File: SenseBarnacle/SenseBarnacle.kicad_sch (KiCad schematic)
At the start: 93 parts, among them J1 USB_B_Mini, J2 Debug, J4 Barrel_Jack, J5 I2C_OLED_Display, J6 Conn_02x35_JumperluxCardEdge, J7 Conn_02x35_JumperluxCardEdge, SW1 USB BOOT, U1 LM324, U13 CH446X, U14 CH446X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

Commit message: started routing
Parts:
- removed R5, R6: 0R, Resistor_SMD:R_0402_1005Metric, symbol JumperlessSymbols:R_Small_US_2
- removed TP17: GPIO_19, symbol Connector:TestPoint
- removed TP18: GPIO_22, symbol Connector:TestPoint
- removed TP19: GPIO_23, symbol Connector:TestPoint
- removed TP8: UART_Rx, symbol Connector:TestPoint
- removed TP9: UART_Tx, symbol Connector:TestPoint
- added C18, C19, C20, C23, C25: 0.1uF, Capacitor_SMD:C_0603_1608Metric_Pad1.08x0.95mm_HandSolder, symbol JumperlessSymbols:C_Small
- added J3: Power, Connector_PinHeader_2.54mm:PinHeader_1x05_P2.54mm_Vertical, symbol Connector:Conn_01x05_Socket
- added R29, R31, R33, R37, R5: 47K, Resistor_SMD:R_0805_2012Metric_Pad1.20x1.40mm_HandSolder, symbol JumperlessSymbols:R_Small_US_3
- added R30, R32, R34, R38, R6: 10K, Resistor_SMD:R_0805_2012Metric_Pad1.20x1.40mm_HandSolder, symbol JumperlessSymbols:R_Small_US_3
- added R35, R36: 2.2K, Resistor_SMD:R_0805_2012Metric_Pad1.20x1.40mm_HandSolder, symbol JumperlessSymbols:R_Small_US_3
- added U4: ~, JumperlessFootprints:Directional_Switch_SKRHADE010, symbol JumperlessSymbols:Switch_Multidirectional
- C1, C13, C2, C8: footprint Capacitor_SMD:C_0603_1608Metric -> Capacitor_SMD:C_0805_2012Metric_Pad1.18x1.45mm_HandSolder
- C10, C11, C12, C3, C4, C5, C9: footprint Capacitor_SMD:C_0402_1005Metric -> Capacitor_SMD:C_0603_1608Metric_Pad1.08x0.95mm_HandSolder
- C21, C22: footprint (none) -> Capacitor_SMD:C_0805_2012Metric_Pad1.18x1.45mm_HandSolder
- J4: footprint (none) -> Connector_BarrelJack:BarrelJack_CUI_PJ-063AH_Horizontal
- J5: footprint (none) -> Connector_PinHeader_2.54mm:PinHeader_1x04_P2.54mm_Vertical
- J6: footprint JumperlessFootprints:HEE70LP03BK_Daughter_Penis -> JumperlessFootprints:HEE70LP03BK_Daughter_Penis_Top
- JP1, JP6: footprint (none) -> JumperlessFootprints:SolderJumper_2_Open_Small
- JP2, JP3, JP4, JP5: footprint (none) -> Jumper:SolderJumper-3_P1.3mm_Bridged2Bar12_RoundedPad1.0x1.5mm
- JP7: footprint (none) -> JumperlessFootprints:SolderJumper_2_Bridged_Small
- R1, R2: footprint Resistor_SMD:R_0402_1005Metric -> Resistor_SMD:R_0402_1005Metric_Pad0.72x0.64mm_HandSolder
- R10, R11, R12, R13, R14, R15, R16, R17, R27, R28: footprint Resistor_SMD:R_0402_1005Metric -> Resistor_SMD:R_0805_2012Metric_Pad1.20x1.40mm_HandSolder
- R18, R19, R20, R21, R22, R23, R24, R25, R26, R3, R8, R9: footprint (none) -> Resistor_SMD:R_0805_2012Metric_Pad1.20x1.40mm_HandSolder
- R4, R7: footprint Resistor_SMD:R_0402_1005Metric -> Resistor_SMD:R_0603_1608Metric_Pad0.98x0.95mm_HandSolder
- TP1, TP10, TP11, TP12, TP14, TP15, TP2, TP20, TP21, TP3, TP4, TP5: footprint (none) -> JumperlessFootprints:TestPoint_D0.75mm
- TP13, TP6, TP7: footprint (none) -> JumperlessFootprints:PINHEADER-1x1_vertical
- TP16: value GPIO_4 -> GPIO_2; footprint (none) -> JumperlessFootprints:TestPoint_D0.75mm
- U1, U2: footprint (none) -> JumperlessFootprints:SOIC-14_3.9x8.7mm_P1.27mm
- U12: footprint (none) -> JumperlessFootprints:QA503C
- U13, U14, U15: footprint (none) -> JumperlessFootprints:LQFP44_Tight
- U6: footprint AK4619VN_AKM -> JumperlessFootprints:AK4619VN_AKM
- U9: footprint RP2040_minimal:RP2040-QFN-56 -> JumperlessFootprints:RP2040-QFN-56
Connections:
- net +18V: now also J3.5 (Pin_5)
- net +3V3: now also J3.2 (Pin_2), R29.2, R31.2, R33.2, R35.1, R36.1, R37.2, R5.2
- net +5V: now also J3.1 (Pin_1)
- net -3.5V: now also J3.4 (Pin_4)
- net GND: now also C18.2, C19.2, C20.2, C23.2, C25.2, J3.3 (Pin_3), U4.5 (Common)
- net I2C_SCL: now also R36.2
- net I2C_SDA: now also R35.2
- net at U9.3 (GPIO1): now also R28.1
- net at U9.2 (GPIO0): now also R27.1
- net GPI0_2: now reaches U9.4 (GPIO2)
- net GPI0_2: now also TP16.1; no longer R27.1
- net SW_A: now reaches U9.5 (GPIO3)
- net SW_A: now also C18.1, R6.1; no longer R28.1
- net GPI0_19 renamed SW_PUSH
- net SW_PUSH: now also C19.1, R30.1
- net GPI0_22 renamed SW_C
- net SW_C: now also C20.1, R32.1
- net GPI0_23 renamed SW_D
- net SW_D: now also C25.1, R38.1
- net GPI0_4 renamed SW_B
- net SW_B: now also C23.1, R34.1; no longer TP16.1
- new net: R29.1, R30.2, U4.2 (Center)
- new net: R37.1, R38.2, U4.6 (D)
- new net: R33.1, R34.2, U4.4 (B)
- new net: R31.1, R32.2, U4.3 (C)
- new net: R5.1, R6.2, U4.1 (A)
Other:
- moved on the sheet: R27, R28

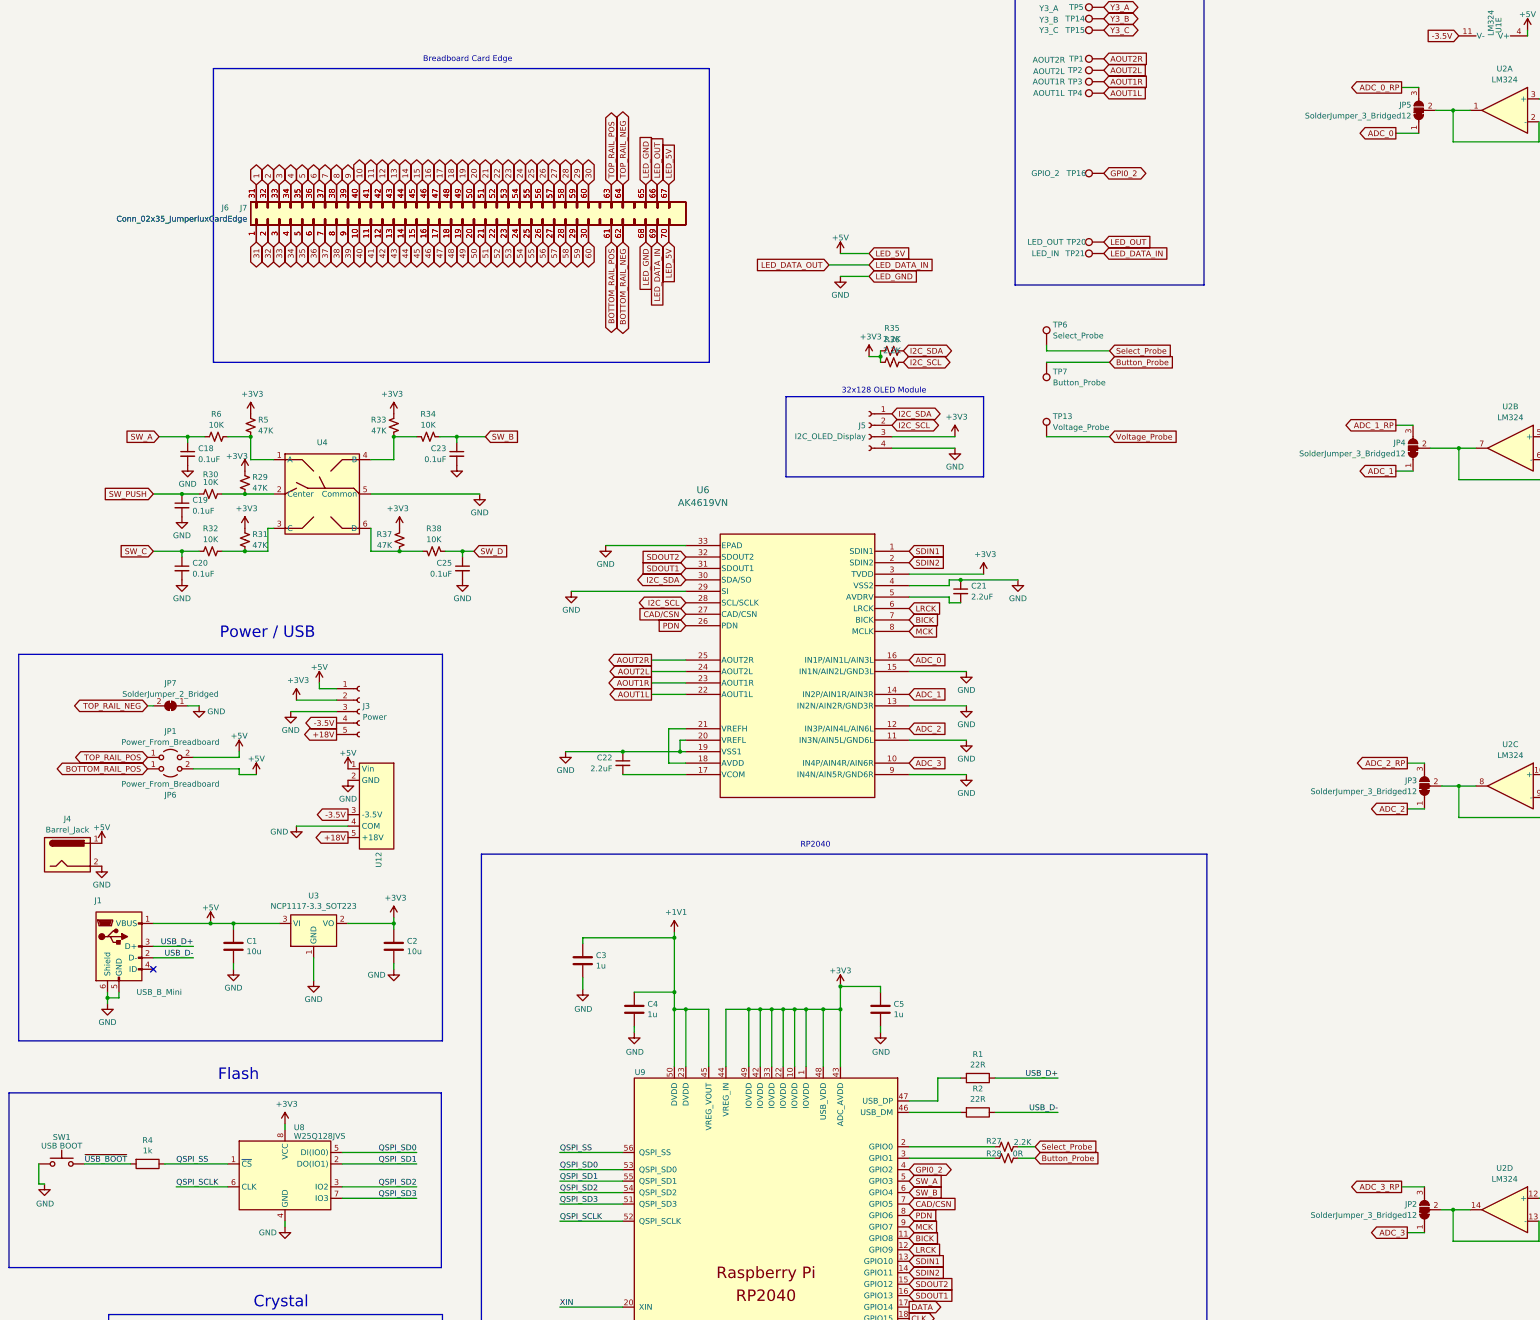
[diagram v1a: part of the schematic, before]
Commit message: add ADC resistors
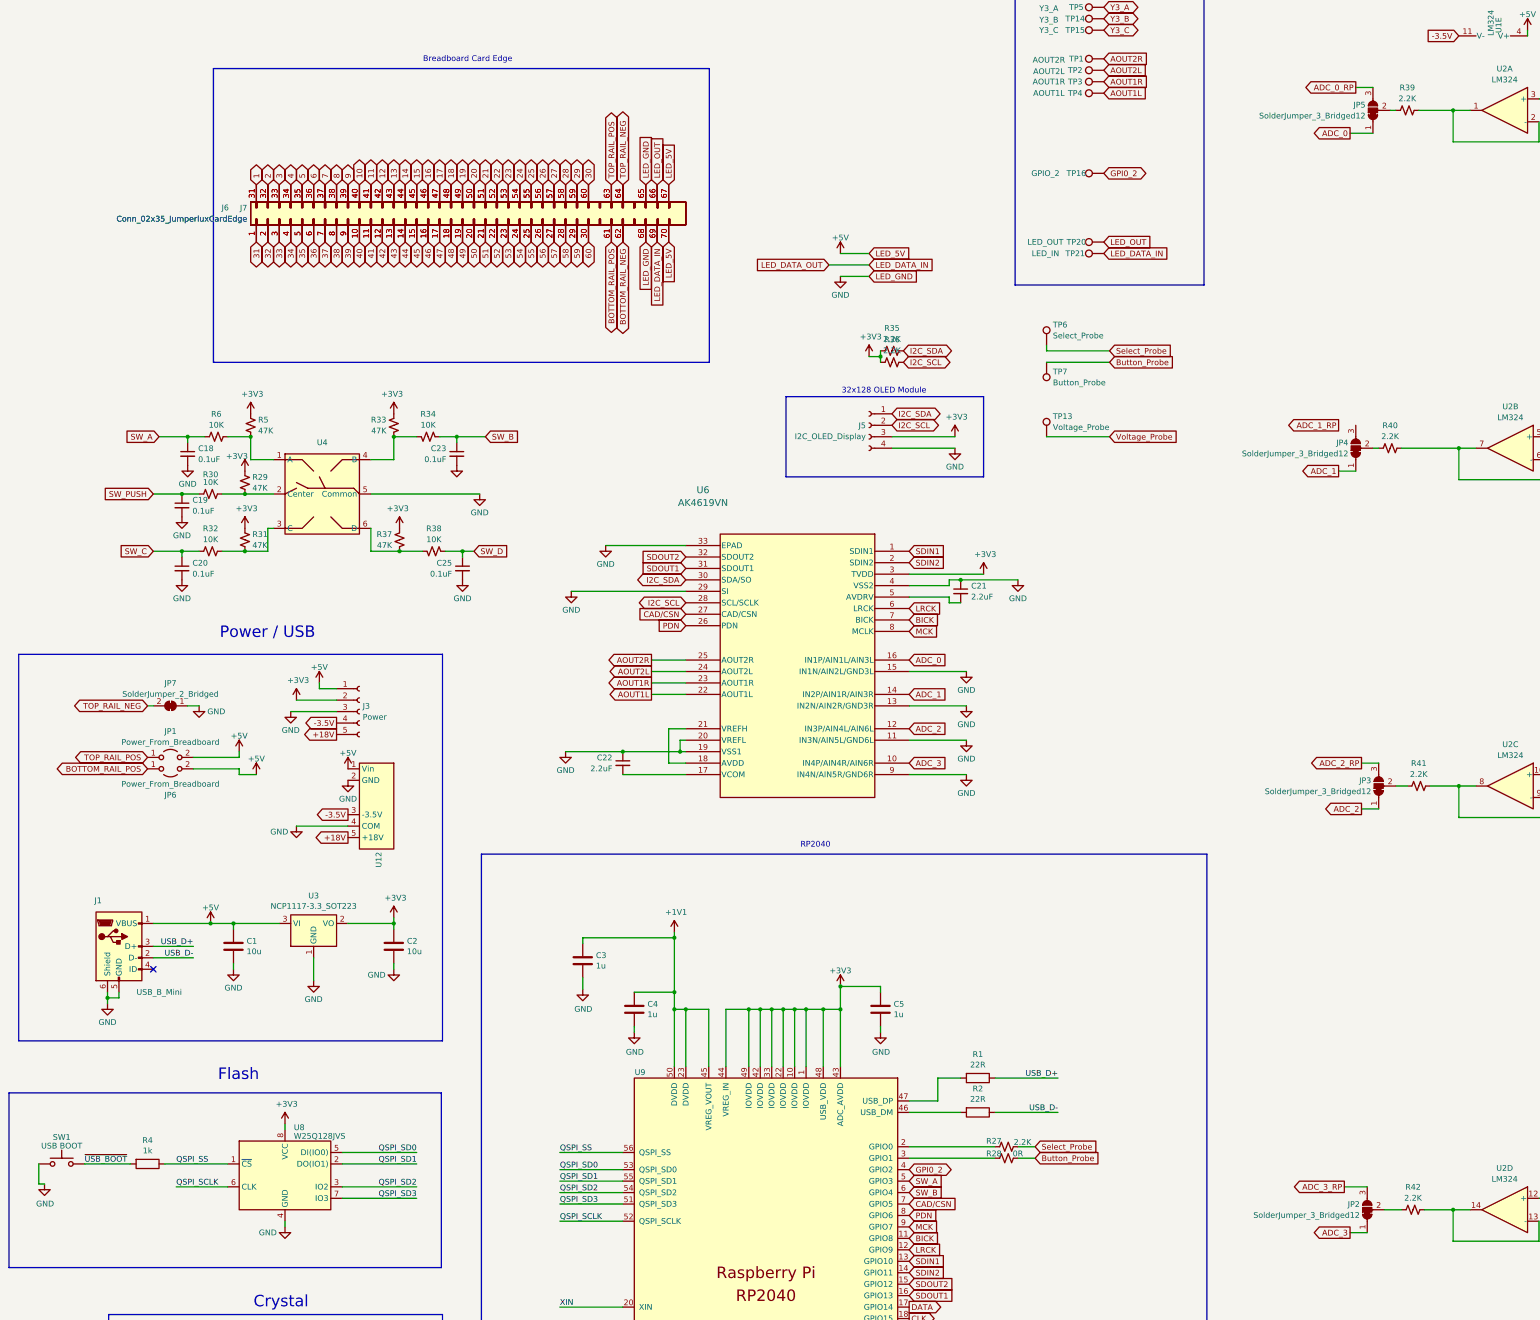
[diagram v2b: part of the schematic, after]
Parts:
- removed J4: Barrel_Jack, Connector_BarrelJack:BarrelJack_CUI_PJ-063AH_Horizontal, symbol Connector:Barrel_Jack
- added R39, R40, R41, R42: 2.2K, Resistor_SMD:R_0805_2012Metric_Pad1.20x1.40mm_HandSolder, symbol JumperlessSymbols:R_Small_US_3
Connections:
- net ADC_1_RP: no longer JP4.3 (B)
- net at U2.1, U2.2 (-): now also R39.2; no longer JP5.2 (C)
- net at U2.6 (-), U2.7: now also R40.2; no longer JP4.2 (C)
- net at U2.13 (-), U2.14: now also R42.2; no longer JP2.2 (C)
- net at U2.8, U2.9 (-): now also R41.2; no longer JP3.2 (C)
- new net: JP2.2 (C), R42.1
- new net: JP3.2 (C), R41.1
- new net: JP5.2 (C), R39.1
- new net: JP4.2 (C), R40.1
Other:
- moved on the sheet: JP2, JP3, JP4, JP5

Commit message: Finished routing
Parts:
- added U5: ~, JumperlessFootprints:QA503C, symbol JumperlessSymbols:QA053C-1803R3
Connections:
- net +18V: now also U5.5 (+18V)
- net +5V: now also U5.1 (Vin)
- net -3.5V: now also U5.3 (-3.5V)
- net ADC_1_RP: now also JP4.3 (B)
- net GND: now also U5.2 (GND), U5.4 (COM)
